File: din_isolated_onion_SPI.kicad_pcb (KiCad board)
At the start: 2 copper layers, 32.5 x 40.5 mm, 11 parts, among them J1 Conn_01x16, J2 Conn_01x16, J3 Conn_01x10, U1 Omega2+, U2 SI8661AB-B-IS1

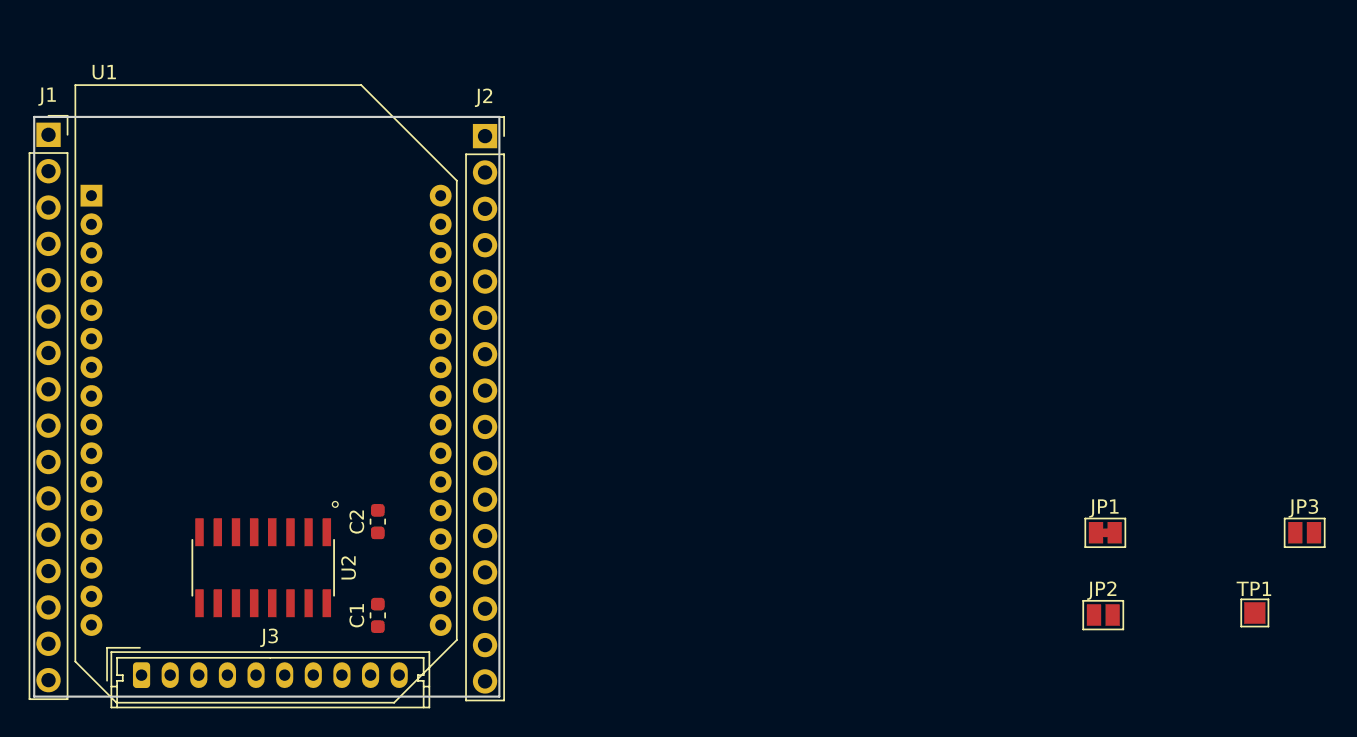
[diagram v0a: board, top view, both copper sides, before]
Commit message: Add pads and renders
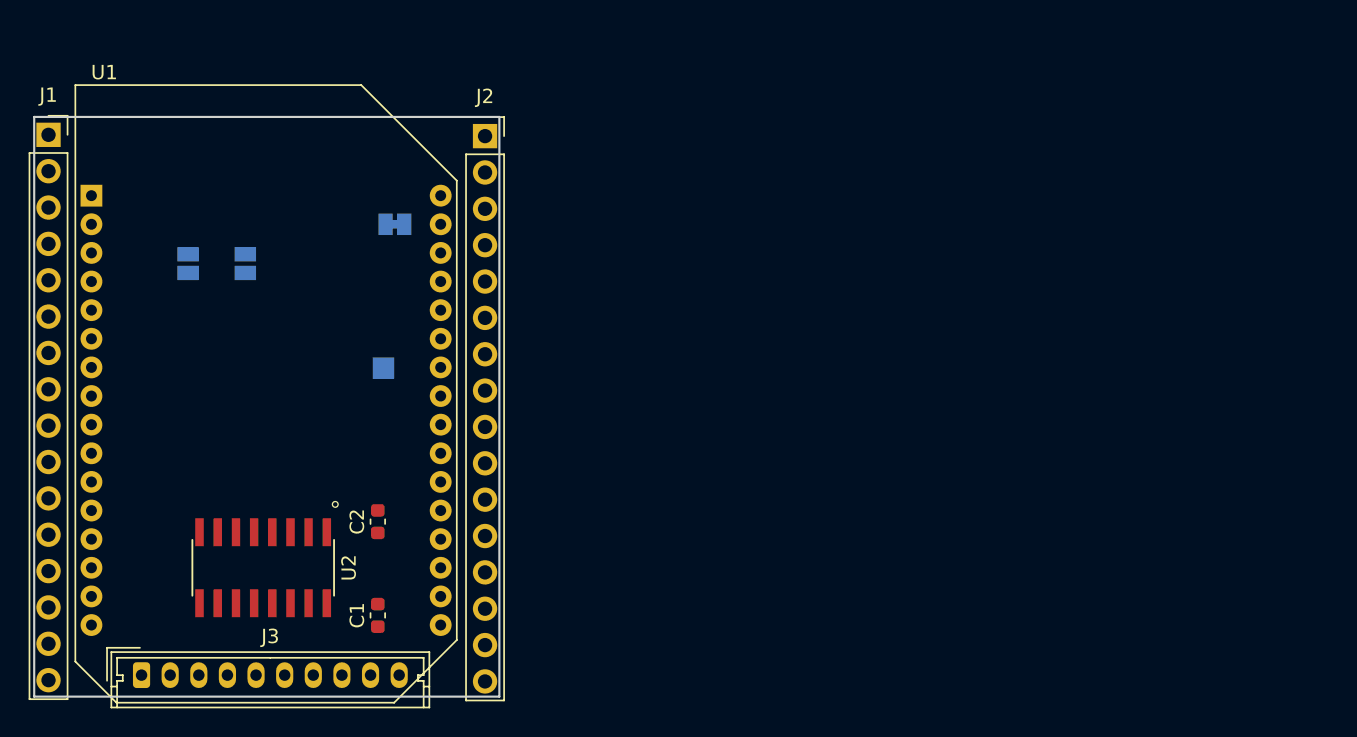
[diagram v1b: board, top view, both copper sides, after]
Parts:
- JP1, JP2, JP3, TP1: moved to B.Cu
- moved JP3 80.2 mm to (140.8, 89.8), turned to 90 degrees
- moved JP2 64.8 mm to (144.8, 89.8), turned to 90 degrees
- moved TP1 63.2 mm to (154.4, 97.0)
- moved JP1 54.1 mm to (155.2, 87.0)
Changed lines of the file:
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@@
     )
   )
-  (module Jumper:SolderJumper-2_P1.3mm_Bridged_Pad1.0x1.5mm (layer F.Cu)
-    (at 204.836905 108.5575)
+  (module Jumper:SolderJumper-2_P1.3mm_Bridged_Pad1.0x1.5mm (layer B.Cu)
+    (at 155.2 87)
     (descr "SMD Solder Jumper, 1x1.5mm Pads, 0.3mm gap, bridged with 1 copper strip")
     (tags "solder jumper open")
     (attr virtual)
-    (fp_text reference JP1 (at 0 -1.8) (layer F.SilkS)
-      (effects (font (size 1 1) (thickness 0.15)))
+    (fp_text reference JP1 (at 0 1.8) (layer B.SilkS)
+      (effects (font (size 1 1) (thickness 0.15)) (justify mirror))
     )
-    (fp_text value Jumper_2_Bridged (at 0 1.9) (layer F.Fab)
-      (effects (font (size 1 1) (thickness 0.15)))
+    (fp_text value Jumper_2_Bridged (at 0 -1.9) (layer B.Fab)
+      (effects (font (size 1 1) (thickness 0.15)) (justify mirror))
     )
-    (fp_poly (pts (xy -0.25 -0.3) (xy 0.25 -0.3) (xy 0.25 0.3) (xy -0.25 0.3)) (layer F.Cu) (width 0))
-    (fp_line (start 1.65 1.25) (end -1.65 1.25) (layer F.CrtYd) (width 0.05))
-    (fp_line (start 1.65 1.25) (end 1.65 -1.25) (layer F.CrtYd) (width 0.05))
-    (fp_line (start -1.65 -1.25) (end -1.65 1.25) (layer F.CrtYd) (width 0.05))
-    (fp_line (start -1.65 -1.25) (end 1.65 -1.25) (layer F.CrtYd) (width 0.05))
-    (fp_line (start -1.4 -1) (end 1.4 -1) (layer F.SilkS) (width 0.12))
-    (fp_line (start 1.4 -1) (end 1.4 1) (layer F.SilkS) (width 0.12))
-    (fp_line (start 1.4 1) (end -1.4 1) (layer F.SilkS) (width 0.12))
-    (fp_line (start -1.4 1) (end -1.4 -1) (layer F.SilkS) (width 0.12))
-    (pad 2 smd rect (at 0.65 0) (size 1 1.5) (layers F.Cu F.Mask)
+    (fp_poly (pts (xy -0.25 0.3) (xy 0.25 0.3) (xy 0.25 -0.3) (xy -0.25 -0.3)) (layer B.Cu) (width 0))
+    (fp_line (start 1.65 -1.25) (end -1.65 -1.25) (layer B.CrtYd) (width 0.05))
+    (fp_line (start 1.65 -1.25) (end 1.65 1.25) (layer B.CrtYd) (width 0.05))
+    (fp_line (start -1.65 1.25) (end -1.65 -1.25) (layer B.CrtYd) (width 0.05))
+    (fp_line (start -1.65 1.25) (end 1.65 1.25) (layer B.CrtYd) (width 0.05))
+    (fp_line (start -1.4 1) (end 1.4 1) (layer B.SilkS) (width 0.12))
+    (fp_line (start 1.4 1) (end 1.4 -1) (layer B.SilkS) (width 0.12))
+    (fp_line (start 1.4 -1) (end -1.4 -1) (layer B.SilkS) (width 0.12))
+    (fp_line (start -1.4 -1) (end -1.4 1) (layer B.SilkS) (width 0.12))
+    (pad 2 smd rect (at 0.65 0) (size 1 1.5) (layers B.Cu B.Mask)
       (net 46 3V3_O))
-    (pad 1 smd rect (at -0.65 0) (size 1 1.5) (layers F.Cu F.Mask)
+    (pad 1 smd rect (at -0.65 0) (size 1 1.5) (layers B.Cu B.Mask)
       (net 41 3V3_C))
   )
-  (module Jumper:SolderJumper-2_P1.3mm_Open_Pad1.0x1.5mm (layer F.Cu)
-    (at 218.764047 108.5575)
+  (module Jumper:SolderJumper-2_P1.3mm_Open_Pad1.0x1.5mm (layer B.Cu)
+    (at 140.75 89.75 90)
     (descr "SMD Solder Jumper, 1x1.5mm Pads, 0.3mm gap, open")
     (tags "solder jumper open")
     (attr virtual)
-    (fp_text reference JP3 (at 0 -1.8) (layer F.SilkS)
-      (effects (font (size 1 1) (thickness 0.15)))
+    (fp_text reference JP3 (at 0 1.8 90) (layer B.SilkS)
+      (effects (font (size 1 1) (thickness 0.15)) (justify mirror))
     )
-    (fp_text value Jumper_NO_Small (at 0 1.9) (layer F.Fab)
-      (effects (font (size 1 1) (thickness 0.15)))
+    (fp_text value Jumper_NO_Small (at 0 -1.9 90) (layer B.Fab)
+      (effects (font (size 1 1) (thickness 0.15)) (justify mirror))
     )
-    (fp_line (start -1.4 1) (end -1.4 -1) (layer F.SilkS) (width 0.12))
-    (fp_line (start 1.4 1) (end -1.4 1) (layer F.SilkS) (width 0.12))
-    (fp_line (start 1.4 -1) (end 1.4 1) (layer F.SilkS) (width 0.12))
-    (fp_line (start -1.4 -1) (end 1.4 -1) (layer F.SilkS) (width 0.12))
-    (fp_line (start -1.65 -1.25) (end 1.65 -1.25) (layer F.CrtYd) (width 0.05))
-    (fp_line (start -1.65 -1.25) (end -1.65 1.25) (layer F.CrtYd) (width 0.05))
-    (fp_line (start 1.65 1.25) (end 1.65 -1.25) (layer F.CrtYd) (width 0.05))
-    (fp_line (start 1.65 1.25) (end -1.65 1.25) (layer F.CrtYd) (width 0.05))
-    (pad 2 smd rect (at 0.65 0) (size 1 1.5) (layers F.Cu F.Mask)
+    (fp_line (start -1.4 -1) (end -1.4 1) (layer B.SilkS) (width 0.12))
+    (fp_line (start 1.4 -1) (end -1.4 -1) (layer B.SilkS) (width 0.12))
+    (fp_line (start 1.4 1) (end 1.4 -1) (layer B.SilkS) (width 0.12))
+    (fp_line (start -1.4 1) (end 1.4 1) (layer B.SilkS) (width 0.12))
+    (fp_line (start -1.65 1.25) (end 1.65 1.25) (layer B.CrtYd) (width 0.05))
+    (fp_line (start -1.65 1.25) (end -1.65 -1.25) (layer B.CrtYd) (width 0.05))
+    (fp_line (start 1.65 -1.25) (end 1.65 1.25) (layer B.CrtYd) (width 0.05))
+    (fp_line (start 1.65 -1.25) (end -1.65 -1.25) (layer B.CrtYd) (width 0.05))
+    (pad 2 smd rect (at 0.65 0 90) (size 1 1.5) (layers B.Cu B.Mask)
       (net 50 "Net-(JP3-Pad2)"))
-    (pad 1 smd rect (at -0.65 0) (size 1 1.5) (layers F.Cu F.Mask)
+    (pad 1 smd rect (at -0.65 0 90) (size 1 1.5) (layers B.Cu B.Mask)
       (net 49 "Net-(JP3-Pad1)"))
   )
-  (module Jumper:SolderJumper-2_P1.3mm_Open_Pad1.0x1.5mm (layer F.Cu)
-    (at 204.694047 114.3075)
+  (module Jumper:SolderJumper-2_P1.3mm_Open_Pad1.0x1.5mm (layer B.Cu)
+    (at 144.75 89.75 90)
     (descr "SMD Solder Jumper, 1x1.5mm Pads, 0.3mm gap, open")
     (tags "solder jumper open")
     (attr virtual)
-    (fp_text reference JP2 (at 0 -1.8) (layer F.SilkS)
-      (effects (font (size 1 1) (thickness 0.15)))
+    (fp_text reference JP2 (at 0 1.8 90) (layer B.SilkS)
+      (effects (font (size 1 1) (thickness 0.15)) (justify mirror))
     )
-    (fp_text value Jumper_NO_Small (at 0 1.9) (layer F.Fab)
-      (effects (font (size 1 1) (thickness 0.15)))
+    (fp_text value Jumper_NO_Small (at 0 -1.9 90) (layer B.Fab)
+      (effects (font (size 1 1) (thickness 0.15)) (justify mirror))
     )
-    (fp_line (start 1.65 1.25) (end -1.65 1.25) (layer F.CrtYd) (width 0.05))
-    (fp_line (start 1.65 1.25) (end 1.65 -1.25) (layer F.CrtYd) (width 0.05))
-    (fp_line (start -1.65 -1.25) (end -1.65 1.25) (layer F.CrtYd) (width 0.05))
-    (fp_line (start -1.65 -1.25) (end 1.65 -1.25) (layer F.CrtYd) (width 0.05))
-    (fp_line (start -1.4 -1) (end 1.4 -1) (layer F.SilkS) (width 0.12))
-    (fp_line (start 1.4 -1) (end 1.4 1) (layer F.SilkS) (width 0.12))
-    (fp_line (start 1.4 1) (end -1.4 1) (layer F.SilkS) (width 0.12))
-    (fp_line (start -1.4 1) (end -1.4 -1) (layer F.SilkS) (width 0.12))
-    (pad 1 smd rect (at -0.65 0) (size 1 1.5) (layers F.Cu F.Mask)
+    (fp_line (start 1.65 -1.25) (end -1.65 -1.25) (layer B.CrtYd) (width 0.05))
+    (fp_line (start 1.65 -1.25) (end 1.65 1.25) (layer B.CrtYd) (width 0.05))
+    (fp_line (start -1.65 1.25) (end -1.65 -1.25) (layer B.CrtYd) (width 0.05))
+    (fp_line (start -1.65 1.25) (end 1.65 1.25) (layer B.CrtYd) (width 0.05))
+    (fp_line (start -1.4 1) (end 1.4 1) (layer B.SilkS) (width 0.12))
+    (fp_line (start 1.4 1) (end 1.4 -1) (layer B.SilkS) (width 0.12))
+    (fp_line (start 1.4 -1) (end -1.4 -1) (layer B.SilkS) (width 0.12))
+    (fp_line (start -1.4 -1) (end -1.4 1) (layer B.SilkS) (width 0.12))
+    (pad 1 smd rect (at -0.65 0 90) (size 1 1.5) (layers B.Cu B.Mask)
       (net 48 "Net-(JP2-Pad1)"))
-    (pad 2 smd rect (at 0.65 0) (size 1 1.5) (layers F.Cu F.Mask)
+    (pad 2 smd rect (at 0.65 0 90) (size 1 1.5) (layers B.Cu B.Mask)
       (net 47 "Net-(JP2-Pad2)"))
   )
-  (module TestPoint:TestPoint_Pad_1.5x1.5mm (layer F.Cu)
-    (at 215.283571 114.1555)
+  (module TestPoint:TestPoint_Pad_1.5x1.5mm (layer B.Cu)
+    (at 154.4 97.05)
     (descr "SMD rectangular pad as test Point, square 1.5mm side length")
     (tags "test point SMD pad rectangle square")
     (attr virtual)
-    (fp_text reference TP1 (at 0 -1.648) (layer F.SilkS)
-      (effects (font (size 1 1) (thickness 0.15)))
+    (fp_text reference TP1 (at 0 1.648) (layer B.SilkS)
+      (effects (font (size 1 1) (thickness 0.15)) (justify mirror))
     )
-    (fp_text value TestPoint (at 0 1.75) (layer F.Fab)
-      (effects (font (size 1 1) (thickness 0.15)))
+    (fp_text value TestPoint (at 0 -1.75) (layer B.Fab)
+      (effects (font (size 1 1) (thickness 0.15)) (justify mirror))
     )
-    (fp_line (start 1.25 1.25) (end -1.25 1.25) (layer F.CrtYd) (width 0.05))
-    (fp_line (start 1.25 1.25) (end 1.25 -1.25) (layer F.CrtYd) (width 0.05))
-    (fp_line (start -1.25 -1.25) (end -1.25 1.25) (layer F.CrtYd) (width 0.05))
-    (fp_line (start -1.25 -1.25) (end 1.25 -1.25) (layer F.CrtYd) (width 0.05))
-    (fp_line (start -0.95 0.95) (end -0.95 -0.95) (layer F.SilkS) (width 0.12))
-    (fp_line (start 0.95 0.95) (end -0.95 0.95) (layer F.SilkS) (width 0.12))
-    (fp_line (start 0.95 -0.95) (end 0.95 0.95) (layer F.SilkS) (width 0.12))
-    (fp_line (start -0.95 -0.95) (end 0.95 -0.95) (layer F.SilkS) (width 0.12))
-    (fp_text user %R (at 0 -1.65) (layer F.Fab)
-      (effects (font (size 1 1) (thickness 0.15)))
+    (fp_line (start 1.25 -1.25) (end -1.25 -1.25) (layer B.CrtYd) (width 0.05))
+    (fp_line (start 1.25 -1.25) (end 1.25 1.25) (layer B.CrtYd) (width 0.05))
+    (fp_line (start -1.25 1.25) (end -1.25 -1.25) (layer B.CrtYd) (width 0.05))
+    (fp_line (start -1.25 1.25) (end 1.25 1.25) (layer B.CrtYd) (width 0.05))
+    (fp_line (start -0.95 -0.95) (end -0.95 0.95) (layer B.SilkS) (width 0.12))
+    (fp_line (start 0.95 -0.95) (end -0.95 -0.95) (layer B.SilkS) (width 0.12))
+    (fp_line (start 0.95 0.95) (end 0.95 -0.95) (layer B.SilkS) (width 0.12))
+    (fp_line (start -0.95 0.95) (end 0.95 0.95) (layer B.SilkS) (width 0.12))
+    (fp_text user %R (at 0 1.65) (layer B.Fab)
+      (effects (font (size 1 1) (thickness 0.15)) (justify mirror))
     )
-    (pad 1 smd rect (at 0 0) (size 1.5 1.5) (layers F.Cu F.Mask)
+    (pad 1 smd rect (at 0 0) (size 1.5 1.5) (layers B.Cu B.Mask)
       (net 45 "Net-(TP1-Pad1)"))
   )

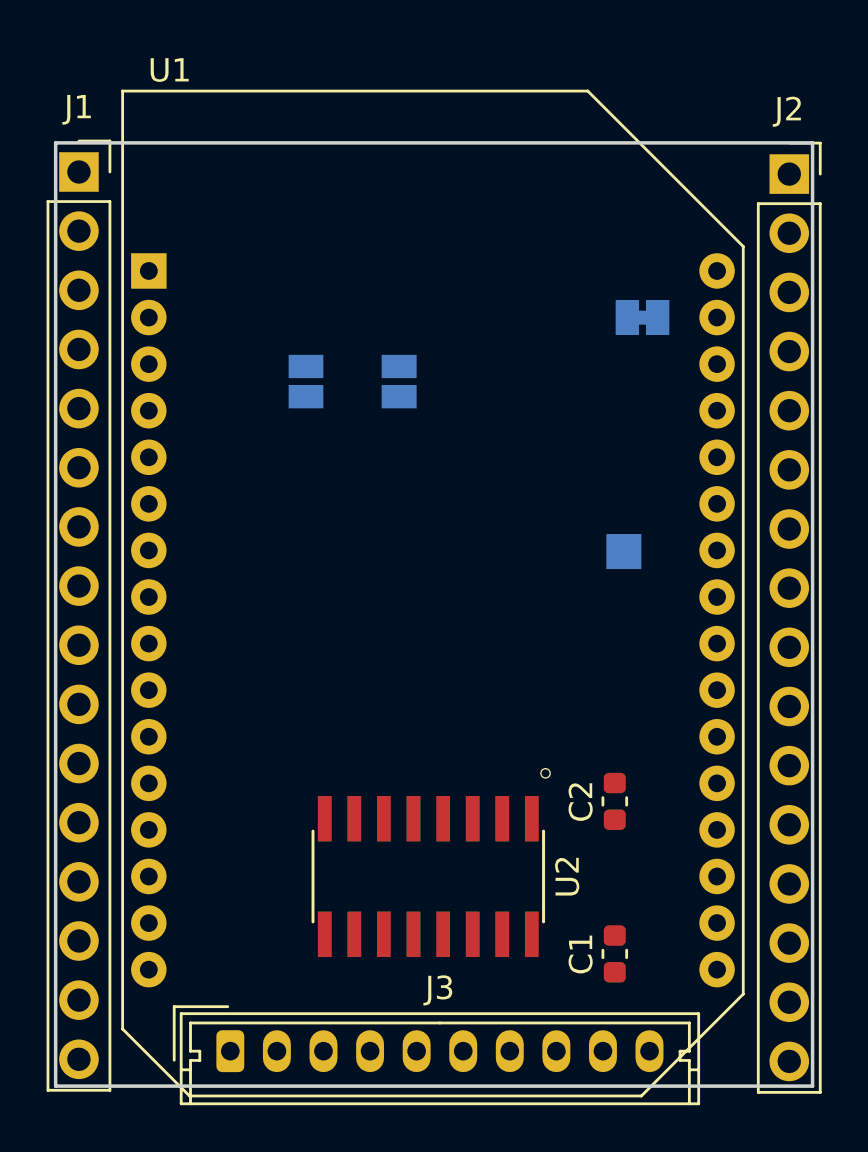
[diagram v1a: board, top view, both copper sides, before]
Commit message: Add GPIO-CS Mux pins
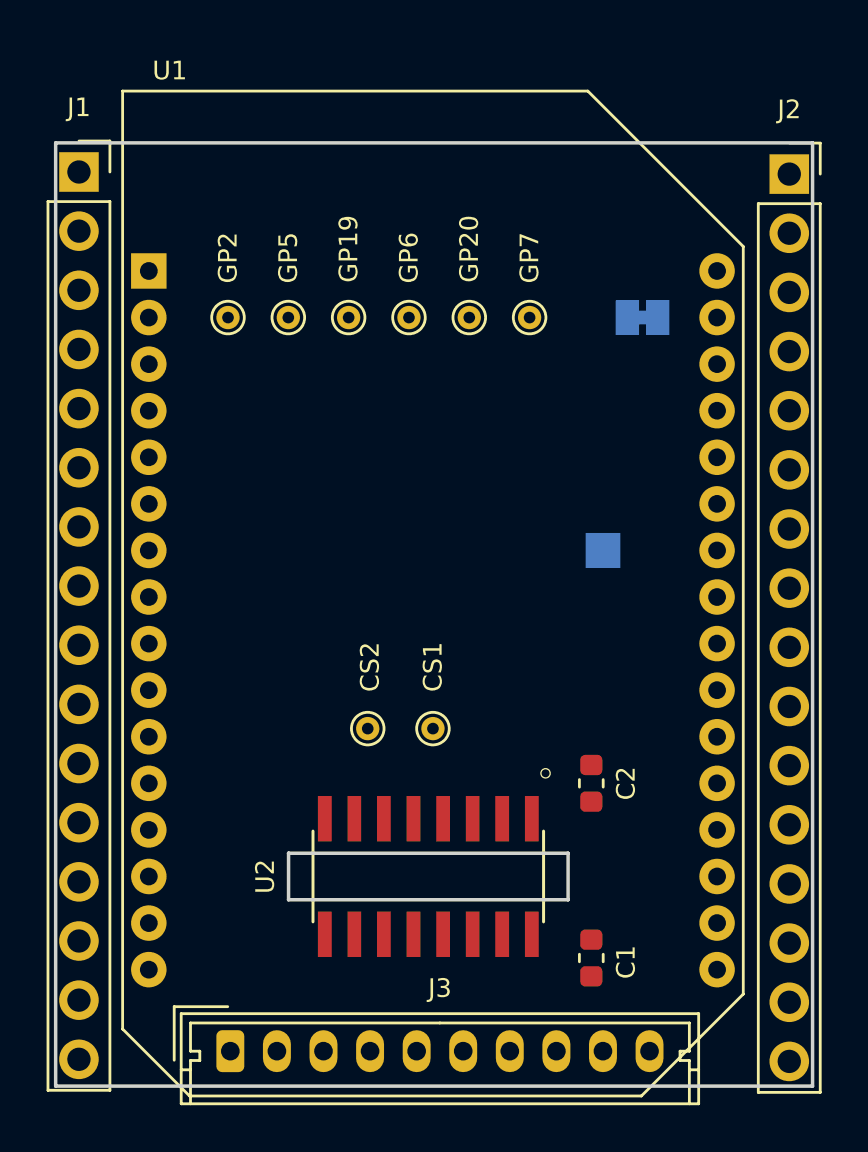
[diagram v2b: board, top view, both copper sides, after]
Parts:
- removed JP2, JP3: Jumper_NO_Small, Jumper:SolderJumper-2_P1.3mm_Open_Pad1.0x1.5mm
- removed TP1: TestPoint, TestPoint:TestPoint_Pad_1.5x1.5mm
- added CS1: TestPoint, TestPoint:TestPoint_THTPad_D1.0mm_Drill0.5mm, F.Cu at (146.2, 104.7)
- added CS2: TestPoint, TestPoint:TestPoint_THTPad_D1.0mm_Drill0.5mm, F.Cu at (143.4, 104.7)
- added FW_RST1: TestPoint, TestPoint:TestPoint_Pad_1.5x1.5mm, B.Cu at (153.5, 97.0)
- added GP19: TestPoint, TestPoint:TestPoint_THTPad_D1.0mm_Drill0.5mm, F.Cu at (142.6, 87.0)
- added GP2: TestPoint, TestPoint:TestPoint_THTPad_D1.0mm_Drill0.5mm, F.Cu at (137.4, 87.0)
- added GP20: TestPoint, TestPoint:TestPoint_THTPad_D1.0mm_Drill0.5mm, F.Cu at (147.8, 87.0)
- added GP5: TestPoint, TestPoint:TestPoint_THTPad_D1.0mm_Drill0.5mm, F.Cu at (140.0, 87.0)
- added GP6: TestPoint, TestPoint:TestPoint_THTPad_D1.0mm_Drill0.5mm, F.Cu at (145.2, 87.0)
- added GP7: TestPoint, TestPoint:TestPoint_THTPad_D1.0mm_Drill0.5mm, F.Cu at (150.3, 87.0)
- moved C2 1.27 mm to (153.0, 107.0)
- moved C1 1.02 mm to (153.0, 114.5)
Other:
- outline, holes or cut-outs redrawn
